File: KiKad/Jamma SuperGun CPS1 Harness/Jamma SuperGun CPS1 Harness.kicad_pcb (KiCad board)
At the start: 2 copper layers, 110.4 x 36 mm, 2 parts

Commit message: updates
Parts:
- renumbered J_FEMALE to J_FEMALE1, J_MALE to J_MALE1
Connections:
- J_FEMALE1 pad 1: (no net) -> /GND
- J_FEMALE1 pad 2: (no net) -> /GND
- J_FEMALE1 pad 3: (no net) -> /+5V
- J_FEMALE1 pad 4: (no net) -> /+5V
- J_FEMALE1 pad 5: (no net) -> /-5V
- J_FEMALE1 pad 6: (no net) -> /+12V
- J_FEMALE1 pad 8: (no net) -> /Coin Counter 1
- J_FEMALE1 pad 9: (no net) -> /Lockout 1
- J_MALE1 pad 1: (no net) -> /GND
- J_MALE1 pad 2: (no net) -> /GND
- J_MALE1 pad 3: (no net) -> /+5V
- J_MALE1 pad 4: (no net) -> /+5V
- J_MALE1 pad 5: (no net) -> /-5V
- J_MALE1 pad 6: (no net) -> /+12V
- J_MALE1 pad 8: (no net) -> /Coin Counter 1
- J_MALE1 pad 9: (no net) -> /Lockout 1
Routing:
- net /GND: track 0.00 -> 162.0 mm
- net /+5V: track 0.00 -> 102.5 mm
- net /-5V: track 0.00 -> 51.3 mm
- net /+12V: track 0.00 -> 51.2 mm
- net /Coin Counter 1: track 0.00 -> 27.0 mm
- net /2P Button 1: track 0.00 -> 26.9 mm
- net /Video Sync: track 0.00 -> 26.9 mm
- net /Video Red: track 0.00 -> 26.9 mm
- net /Video Green: track 0.00 -> 26.9 mm
- net /Video GND: track 0.00 -> 26.9 mm
- net /Video Blue: track 0.00 -> 26.9 mm
- net /Tilt Switch: track 0.00 -> 26.9 mm
- net /Test Switch: track 0.00 -> 26.9 mm
- net /Speaker-: track 0.00 -> 26.9 mm
- net /Speaker+: track 0.00 -> 26.9 mm
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
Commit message: updates
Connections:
- net /1P Button 1 renamed /1P_LP
- net /1P Button 2 renamed /1P_MP
- net /2P Button 1 renamed /2P_LP
- net /2P Button 2 renamed /2P_MP
- J_FEMALE1 pad 24: /1P Button 3 -> /1P_HP
- J_FEMALE1 pad b: /2P Button 3 -> /2P_HP
- J_MALE1 pad 24: /1P Button 3 -> /1P_LK
- J_MALE1 pad 25: /N/C -> /1P_MK
- J_MALE1 pad 26: /N/C -> /1P_HP
- J_MALE1 pad 27: /GND -> /1P_HK
- J_MALE1 pad b: /2P Button 3 -> /2P_LK
- J_MALE1 pad c: /N/C -> /2P_MK
- J_MALE1 pad d: /N/C -> /2P_HP
- J_MALE1 pad e: /GND -> /2P_HK
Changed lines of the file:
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@@
 			(size 2.35 8)
 			(layers "F.Cu" "F.Mask" "F.Paste")
-			(net "/1P Button 1")
+			(net "/1P_LP")
 			(pinfunction "22_22")
 			(pintype "input")
@@
 			(size 2.35 8)
 			(layers "F.Cu" "F.Mask" "F.Paste")
-			(net "/1P Button 2")
+			(net "/1P_MP")
 			(pinfunction "23_23")
 			(pintype "input")
@@
 			(size 2.35 8)
 			(layers "F.Cu" "F.Mask" "F.Paste")
-			(net "/1P Button 3")
+			(net "/1P_HP")
 			(pinfunction "24_24")
 			(pintype "input")
@@
 			(size 2.35 8)
 			(layers "F.Mask" "B.Cu" "F.Paste")
-			(net "/2P Button 1")
+			(net "/2P_LP")
 			(pinfunction "Z_Z")
 			(pintype "input")
@@
 			(size 2.35 8)
 			(layers "F.Mask" "B.Cu" "F.Paste")
-			(net "/2P Button 2")
+			(net "/2P_MP")
 			(pinfunction "a_a")
 			(pintype "input")
@@
 			(size 2.35 8)
 			(layers "F.Mask" "B.Cu" "F.Paste")
-			(net "/2P Button 3")
+			(net "/2P_HP")
 			(pinfunction "b_b")
 			(pintype "input")
@@
 			(size 2.35 8)
 			(layers "F.Cu" "F.Mask" "F.Paste")
-			(net "/1P Button 1")
+			(net "/1P_LP")
 			(pinfunction "22_22")
 			(pintype "input")
@@
 			(size 2.35 8)
 			(layers "F.Cu" "F.Mask" "F.Paste")
-			(net "/1P Button 2")
+			(net "/1P_MP")
 			(pinfunction "23_23")
 			(pintype "input")
@@
 			(size 2.35 8)
 			(layers "F.Cu" "F.Mask" "F.Paste")
-			(net "/1P Button 3")
+			(net "/1P_LK")
 			(pinfunction "24_24")
 			(pintype "input")
@@
 			(size 2.35 8)
 			(layers "F.Cu" "F.Mask" "F.Paste")
-			(net "/N{slash}C")
+			(net "/1P_MK")
 			(pinfunction "25_25")
 			(pintype "input")
@@
 			(size 2.35 8)
 			(layers "F.Cu" "F.Mask" "F.Paste")
-			(net "/N{slash}C")
+			(net "/1P_HP")
 			(pinfunction "26_26")
 			(pintype "input")
@@
 			(size 2.35 8)
 			(layers "F.Cu" "F.Mask" "F.Paste")
-			(net "/GND")
+			(net "/1P_HK")
 			(pinfunction "27_27")
 			(pintype "input")
@@
 			(size 2.35 8)
 			(layers "F.Mask" "B.Cu" "F.Paste")
-			(net "/2P Button 1")
+			(net "/2P_LP")
 			(pinfunction "Z_Z")
 			(pintype "input")
@@
 			(size 2.35 8)
 			(layers "F.Mask" "B.Cu" "F.Paste")
-			(net "/2P Button 2")
+			(net "/2P_MP")
 			(pinfunction "a_a")
 			(pintype "input")
@@
 			(size 2.35 8)
 			(layers "F.Mask" "B.Cu" "F.Paste")
-			(net "/2P Button 3")
+			(net "/2P_LK")
 			(pinfunction "b_b")
 			(pintype "input")
@@
 			(size 2.35 8)
 			(layers "F.Mask" "B.Cu" "F.Paste")
-			(net "/N{slash}C")
+			(net "/2P_MK")
 			(pinfunction "c_c")
 			(pintype "input")
@@
 			(size 2.35 8)
 			(layers "F.Mask" "B.Cu" "F.Paste")
-			(net "/N{slash}C")
+			(net "/2P_HP")
 			(pinfunction "d_d")
 			(pintype "input")
@@
 			(size 2.35 8)
 			(layers "F.Mask" "B.Cu" "F.Paste")
-			(net "/GND")
+			(net "/2P_HK")
 			(pinfunction "e_e")
 			(pintype "input")
@@
 	)
 	(segment
-		(start 179.39 46)
-		(end 179.39 72.9)
-		(width 0.4)
-		(layer "F.Cu")
-		(net "/Speaker+")
-	)
-	(segment
-		(start 183.35 46)
-		(end 183.35 72.9)
-		(width 0.4)
-		(layer "F.Cu")
-		(net "/Audio+")
-	)
-	(segment
-		(start 187.31 46)
-		(end 187.31 72.9)
-		(width 0.4)
-		(layer "F.Cu")
-		(net "/Video Red")
-	)
-	(segment
-		(start 191.27 46)
-		(end 191.27 72.9)
-		(width 0.4)
-		(layer "F.Cu")
-		(net "/Video Blue")
-	)
-	(segment
-		(start 195.23 46)
-		(end 195.23 72.9)
-		(width 0.4)
-		(layer "F.Cu")
-		(net "/Video GND")
-	)
-	(segment
-		(start 199.19 46)
-		(end 199.19 72.9)
-		(width 0.4)
-		(layer "F.Cu")
-		(net "/Test Switch")
-	)
-	(segment
-		(start 203.15 46)
-		(end 203.15 72.9)
-		(width 0.4)
-		(layer "F.Cu")
-		(net "/1P Coin")
-	)
-	(segment
-		(start 207.11 46)
-		(end 207.11 72.9)
-		(width 0.4)
-		(layer "F.Cu")
-		(net "/1P Start")
-	)
-	(segment
-		(start 211.07 46)
-		(end 211.07 72.9)
-		(width 0.4)
-		(layer "F.Cu")
-		(net "/1P Up")
-	)
-	(segment
-		(start 215.03 46)
-		(end 215.03 72.9)
-		(width 0.4)
-		(layer "F.Cu")
-		(net "/1P Down")
-	)
-	(segment
-		(start 218.99 46)
-		(end 218.99 72.9)
-		(width 0.4)
-		(layer "F.Cu")
-		(net "/1P Left")
-	)
-	(segment
-		(start 222.95 46)
-		(end 222.95 72.9)
-		(width 0.4)
-		(layer "F.Cu")
-		(net "/1P Right")
-	)
-	(segment
-		(start 226.91 46)
-		(end 226.91 72.9)
-		(width 0.4)
-		(layer "F.Cu")
-		(net "/1P Button 1")
-	)
-	(segment
-		(start 230.87 46)
-		(end 230.87 72.9)
-		(width 0.4)
-		(layer "F.Cu")
-		(net "/1P Button 2")
-	)
-	(segment
 		(start 147.6 48.525)
 		(end 147.6 72.875)
@@
 	)
 	(segment
+		(start 171.47 46.03)
+		(end 171.4 46.1)
+		(width 0.2)
+		(layer "F.Cu")
+		(net "/Coin Counter 1")
+	)
+	(segment
+		(start 171.4 46.1)
+		(end 171.47 46.17)
+		(width 0.2)
+		(layer "F.Cu")
+		(net "/Coin Counter 1")
+	)
+	(segment
+		(start 171.47 46)
+		(end 171.47 46.03)
+		(width 0.2)
+		(layer "F.Cu")
+		(net "/Coin Counter 1")
+	)
+	(segment
+		(start 171.47 46.17)
+		(end 171.47 72.9)
+		(width 0.4)
+		(layer "F.Cu")
+		(net "/Coin Counter 1")
+	)
+	(segment
+		(start 175.43 46)
+		(end 175.43 72.9)
+		(width 0.4)
+		(layer "F.Cu")
+		(net "/Lockout 1")
+	)
+	(segment
+		(start 179.39 46)
+		(end 179.39 72.9)
+		(width 0.4)
+		(layer "F.Cu")
+		(net "/Speaker+")
+	)
+	(segment
+		(start 183.35 46)
+		(end 183.35 72.9)
+		(width 0.4)
+		(layer "F.Cu")
+		(net "/Audio+")
+	)
+	(segment
+		(start 187.31 46)
+		(end 187.31 72.9)
+		(width 0.4)
+		(layer "F.Cu")
+		(net "/Video Red")
+	)
+	(segment
+		(start 191.27 46)
+		(end 191.27 72.9)
+		(width 0.4)
+		(layer "F.Cu")
+		(net "/Video Blue")
+	)
+	(segment
+		(start 195.23 46)
+		(end 195.23 72.9)
+		(width 0.4)
+		(layer "F.Cu")
+		(net "/Video GND")
+	)
+	(segment
+		(start 199.19 46)
+		(end 199.19 72.9)
+		(width 0.4)
+		(layer "F.Cu")
+		(net "/Test Switch")
+	)
+	(segment
+		(start 203.15 46)
+		(end 203.15 72.9)
+		(width 0.4)
+		(layer "F.Cu")
+		(net "/1P Coin")
+	)
+	(segment
+		(start 207.11 46)
+		(end 207.11 72.9)
+		(width 0.4)
+		(layer "F.Cu")
+		(net "/1P Start")
+	)
+	(segment
+		(start 211.07 46)
+		(end 211.07 72.9)
+		(width 0.4)
+		(layer "F.Cu")
+		(net "/1P Up")
+	)
+	(segment
+		(start 215.03 46)
+		(end 215.03 72.9)
+		(width 0.4)
+		(layer "F.Cu")
+		(net "/1P Down")
+	)
+	(segment
+		(start 218.99 46)
+		(end 218.99 72.9)
+		(width 0.4)
+		(layer "F.Cu")
+		(net "/1P Left")
+	)
+	(segment
+		(start 222.95 46)
+		(end 222.95 72.9)
+		(width 0.4)
+		(layer "F.Cu")
+		(net "/1P Right")
+	)
+	(segment
 		(start 171.47 46)
 		(end 171.47 72.9)
@@
 		(width 0.4)
 		(layer "B.Cu")
-		(net "/2P Button 1")
+		(net "/2P_LP")
 	)
 	(segment
@@
 		(width 0.2)
 		(layer "B.Cu")
-		(net "/2P Button 1")
+		(net "/2P_LP")
 	)
 	(segment
@@
 		(width 0.2)
 		(layer "B.Cu")
-		(net "/2P Button 1")
+		(net "/2P_LP")
 	)
 	(segment
@@
 		(width 0.2)
 		(layer "B.Cu")
-		(net "/2P Button 1")
+		(net "/2P_LP")
+	)
+	(segment
+		(start 226.91 46)
+		(end 226.91 72.9)
+		(width 0.4)
+		(layer "F.Cu")
+		(net "/1P_LP")
 	)
 	(segment
@@
 		(width 0.4)
 		(layer "B.Cu")
-		(net "/2P Button 2")
-	)
-	(segment
-		(start 175.43 46)
-		(end 175.43 72.9)
-		(width 0.4)
-		(layer "F.Cu")
-		(net "/Lockout 1")
-	)
-	(segment
-		(start 171.47 46.03)
-		(end 171.4 46.1)
-		(width 0.2)
-		(layer "F.Cu")
-		(net "/Coin Counter 1")
-	)
-	(segment
-		(start 171.4 46.1)
-		(end 171.47 46.17)
-		(width 0.2)
-		(layer "F.Cu")
-		(net "/Coin Counter 1")
-	)
-	(segment
-		(start 171.47 46)
-		(end 171.47 46.03)
-		(width 0.2)
-		(layer "F.Cu")
-		(net "/Coin Counter 1")
-	)
-	(segment
-		(start 171.47 46.17)
-		(end 171.47 72.9)
-		(width 0.4)
-		(layer "F.Cu")
-		(net "/Coin Counter 1")
+		(net "/2P_MP")
+	)
+	(segment
+		(start 230.87 46)
+		(end 230.87 72.9)
+		(width 0.4)
+		(layer "F.Cu")
+		(net "/1P_MP")
 	)
 	(embedded_fonts no)

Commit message: updates
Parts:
- added CPS1_KH1: ~, Connector_JST:JST_EH_B10B-EH-A_1x10_P2.50mm_Vertical, F.Cu at (249.1, 58.8)
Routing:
- net /2P_HP: track 0.00 -> 61.5 mm
- net /1P_HP: track 0.00 -> 60.4 mm, vias 0 -> 2
- net /2P_HK: track 0.00 -> 28.0 mm
- net /1P_MP: track 26.9 -> 48.9 mm
- net /2P_MP: track 26.9 -> 48.3 mm
- net /1P_HK: track 0.00 -> 19.8 mm, vias 0 -> 2
- net /2P_MK: track 0.00 -> 19.7 mm, vias 0 -> 2
- net /1P_LK: track 0.00 -> 18.1 mm
- net /1P_MK: track 0.00 -> 17.2 mm, vias 0 -> 2
- net /1P_LP: track 26.9 -> 44.0 mm
- net /2P_LP: track 26.9 -> 44.0 mm
- net /1P Right: track 26.9 -> 41.1 mm
- net /2P Right: track 26.9 -> 41.1 mm
- net /2P_LK: track 0.00 -> 13.1 mm, vias 0 -> 2
- net /GND: track 162.0 -> 170.1 mm
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
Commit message: updates
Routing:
- net /1P_MP: track 48.9 -> 48.3 mm
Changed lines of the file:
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@@
+	)
+	(segment
+		(start 222.43 66.43)
+		(end 222.95 66.95)
+		(width 0.4)
+		(layer "F.Cu")
+		(net "/1P Right")
+	)
+	(segment
+		(start 216.48 66.43)
+		(end 222.43 66.43)
+		(width 0.4)
+		(layer "F.Cu")
+		(net "/1P Right")
+	)
+	(segment
+		(start 222.95 66.95)
+		(end 222.95 72.9)
+		(width 0.4)
+		(layer "F.Cu")
+		(net "/1P Right")
+	)
+	(segment
+		(start 213.57 55.38)
+		(end 213.57 63.52)
+		(width 0.4)
+		(layer "F.Cu")
+		(net "/1P Right")
 	)
 	(segment
@@
 	)
 	(segment
-		(start 216.05 66)
-		(end 222 66)
+		(start 213.57 63.52)
+		(end 216.48 66.43)
+		(width 0.4)
+		(layer "F.Cu")
+		(net "/1P Right")
+	)
+	(segment
+		(start 217.95 51)
+		(end 213.57 55.38)
 		(width 0.4)
 		(layer "F.Cu")
@@
 	)
 	(segment
-		(start 213.57 63.52)
-		(end 216.05 66)
-		(width 0.4)
-		(layer "F.Cu")
-		(net "/1P Right")
-	)
-	(segment
-		(start 213.57 55.38)
-		(end 213.57 63.52)
-		(width 0.4)
-		(layer "F.Cu")
-		(net "/1P Right")
-	)
-	(segment
-		(start 222.95 66.95)
-		(end 222.95 72.9)
-		(width 0.4)
-		(layer "F.Cu")
-		(net "/1P Right")
-	)
-	(segment
-		(start 217.95 51)
-		(end 213.57 55.38)
-		(width 0.4)
-		(layer "F.Cu")
-		(net "/1P Right")
-	)
-	(segment
-		(start 222 66)
-		(end 222.95 66.95)
-		(width 0.4)
-		(layer "F.Cu")
-		(net "/1P Right")
+		(start 226.91 46)
+		(end 226.91 50.296)
+		(width 0.4)
+		(layer "F.Cu")
+		(net "/1P_LP")
+	)
+	(segment
+		(start 214.84 62.84)
+		(end 217 65)
+		(width 0.4)
+		(layer "F.Cu")
+		(net "/1P_LP")
+	)
+	(segment
+		(start 225.206 52)
+		(end 219.182 52)
+		(width 0.4)
+		(layer "F.Cu")
+		(net "/1P_LP")
 	)
 	(segment
@@
 	)
 	(segment
+		(start 226.91 68.91)
+		(end 226.91 72.9)
+		(width 0.4)
+		(layer "F.Cu")
+		(net "/1P_LP")
+	)
+	(segment
 		(start 217 65)
 		(end 223 65)
@@
 	)
 	(segment
-		(start 214.84 62.84)
-		(end 217 65)
-		(width 0.4)
-		(layer "F.Cu")
-		(net "/1P_LP")
-	)
-	(segment
-		(start 214.84 56.16)
-		(end 214.84 62.84)
-		(width 0.4)
-		(layer "F.Cu")
-		(net "/1P_LP")
-	)
-	(segment
-		(start 225.206 52)
-		(end 219 52)
-		(width 0.4)
-		(layer "F.Cu")
-		(net "/1P_LP")
-	)
-	(segment
-		(start 226.91 46)
-		(end 226.91 50.296)
-		(width 0.4)
-		(layer "F.Cu")
-		(net "/1P_LP")
-	)
-	(segment
-		(start 226.91 68.91)
-		(end 226.91 72.9)
-		(width 0.4)
-		(layer "F.Cu")
-		(net "/1P_LP")
-	)
-	(segment
-		(start 219 52)
-		(end 214.84 56.16)
+		(start 219.182 52)
+		(end 214.84 56.342)
 		(width 0.4)
 		(layer "F.Cu")
@@
 	)
 	(segment
+		(start 214.84 56.342)
+		(end 214.84 62.84)
+		(width 0.4)
+		(layer "F.Cu")
+		(net "/1P_LP")
+	)
+	(segment
+		(start 218.638528 63.89)
+		(end 226.016 63.89)
+		(width 0.4)
+		(layer "F.Cu")
+		(net "/1P_MP")
+	)
+	(segment
 		(start 219.4812 53.0188)
 		(end 216.11 56.39)
@@
 	)
 	(segment
-		(start 218.536928 63.7884)
-		(end 225.9144 63.7884)
-		(width 0.4)
-		(layer "F.Cu")
-		(net "/1P_MP")
-	)
-	(segment
-		(start 230.87 50.908)
-		(end 228.7592 53.0188)
+		(start 226.016 63.89)
+		(end 230.87 68.744)
+		(width 0.4)
+		(layer "F.Cu")
+		(net "/1P_MP")
+	)
+	(segment
+		(start 230.87 49.892)
+		(end 227.7432 53.0188)
+		(width 0.4)
+		(layer "F.Cu")
+		(net "/1P_MP")
+	)
+	(segment
+		(start 227.7432 53.0188)
+		(end 219.4812 53.0188)
+		(width 0.4)
+		(layer "F.Cu")
+		(net "/1P_MP")
+	)
+	(segment
+		(start 216.11 61.361472)
+		(end 218.638528 63.89)
 		(width 0.4)
 		(layer "F.Cu")
@@
 	(segment
 		(start 230.87 46)
-		(end 230.87 50.908)
-		(width 0.4)
-		(layer "F.Cu")
-		(net "/1P_MP")
-	)
-	(segment
-		(start 228.7592 53.0188)
-		(end 219.4812 53.0188)
-		(width 0.4)
-		(layer "F.Cu")
-		(net "/1P_MP")
-	)
-	(segment
-		(start 216.11 61.361472)
-		(end 218.536928 63.7884)
-		(width 0.4)
-		(layer "F.Cu")
-		(net "/1P_MP")
-	)
-	(segment
-		(start 225.9144 63.7884)
-		(end 230.87 68.744)
+		(end 230.87 49.892)
 		(width 0.4)
 		(layer "F.Cu")
@@
 	)
 	(segment
-		(start 216.05 66)
-		(end 222.03 66)
+		(start 213.57 63.52)
+		(end 216.48 66.43)
+		(width 0.4)
+		(layer "B.Cu")
+		(net "/2P Right")
+	)
+	(segment
+		(start 222.95 66.92)
+		(end 222.95 72.9)
+		(width 0.4)
+		(layer "B.Cu")
+		(net "/2P Right")
+	)
+	(segment
+		(start 216.48 66.43)
+		(end 222.46 66.43)
+		(width 0.4)
+		(layer "B.Cu")
+		(net "/2P Right")
+	)
+	(segment
+		(start 222.95 46)
+		(end 222.95 51)
+		(width 0.4)
+		(layer "B.Cu")
+		(net "/2P Right")
+	)
+	(segment
+		(start 222.46 66.43)
+		(end 222.95 66.92)
+		(width 0.4)
+		(layer "B.Cu")
+		(net "/2P Right")
+	)
+	(segment
+		(start 218 51)
+		(end 213.57 55.43)
+		(width 0.4)
+		(layer "B.Cu")
+		(net "/2P Right")
+	)
+	(segment
+		(start 222.95 51)
+		(end 218 51)
 		(width 0.4)
 		(layer "B.Cu")
@@
 		(width 0.4)
 		(layer "B.Cu")
-		(net "/2P Right")
-	)
-	(segment
-		(start 222.03 66)
-		(end 222.95 66.92)
-		(width 0.4)
-		(layer "B.Cu")
-		(net "/2P Right")
-	)
-	(segment
-		(start 213.57 63.52)
-		(end 216.05 66)
-		(width 0.4)
-		(layer "B.Cu")
-		(net "/2P Right")
-	)
-	(segment
-		(start 222.95 51)
-		(end 218 51)
-		(width 0.4)
-		(layer "B.Cu")
-		(net "/2P Right")
-	)
-	(segment
-		(start 218 51)
-		(end 213.57 55.43)
-		(width 0.4)
-		(layer "B.Cu")
-		(net "/2P Right")
-	)
-	(segment
-		(start 222.95 66.92)
-		(end 222.95 72.9)
-		(width 0.4)
-		(layer "B.Cu")
-		(net "/2P Right")
-	)
-	(segment
-		(start 222.95 46)
-		(end 222.95 51)
-		(width 0.4)
-		(layer "B.Cu")

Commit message: updates
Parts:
- moved CPS1_KH1 3.45 mm to (245.9, 60.1)
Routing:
- net /GND: track 170.1 -> 202.2 mm
- net /2P_LK: track 13.1 -> 19.2 mm
- net /1P_MK: track 17.2 -> 22.2 mm
- net /1P_HK: track 19.8 -> 22.3 mm
- net /2P_HK: track 28.0 -> 30.3 mm

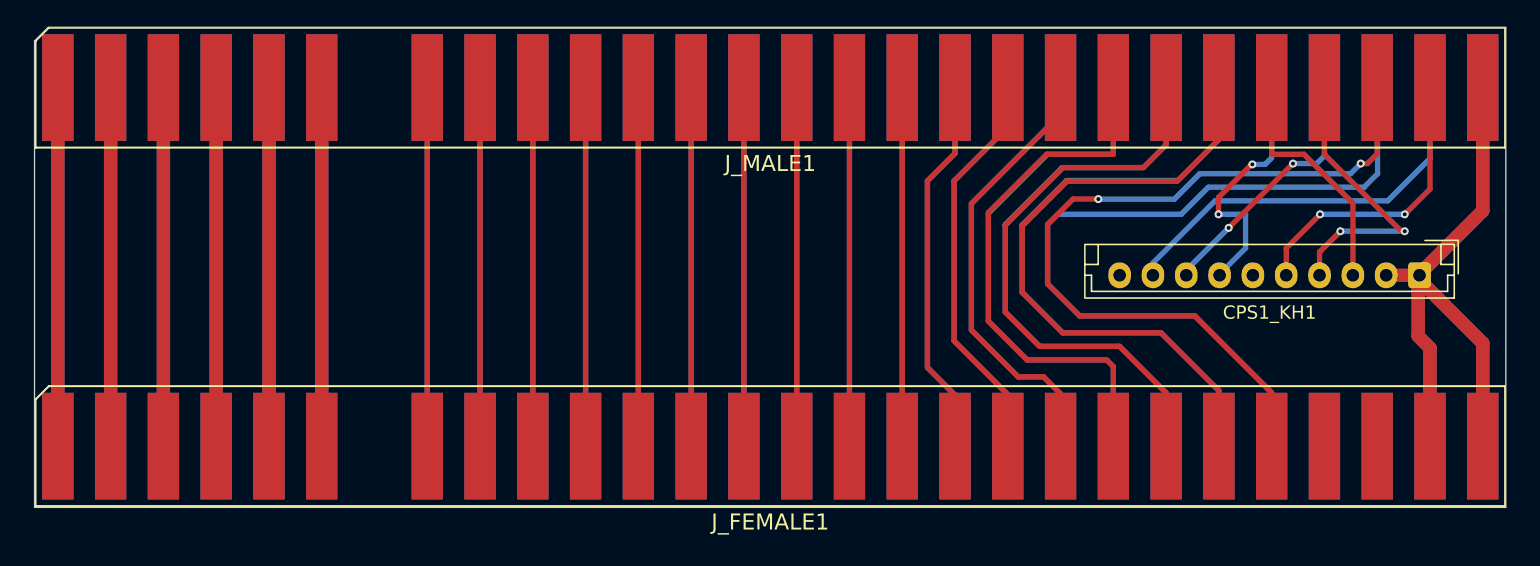
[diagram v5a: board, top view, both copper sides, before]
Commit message: update size
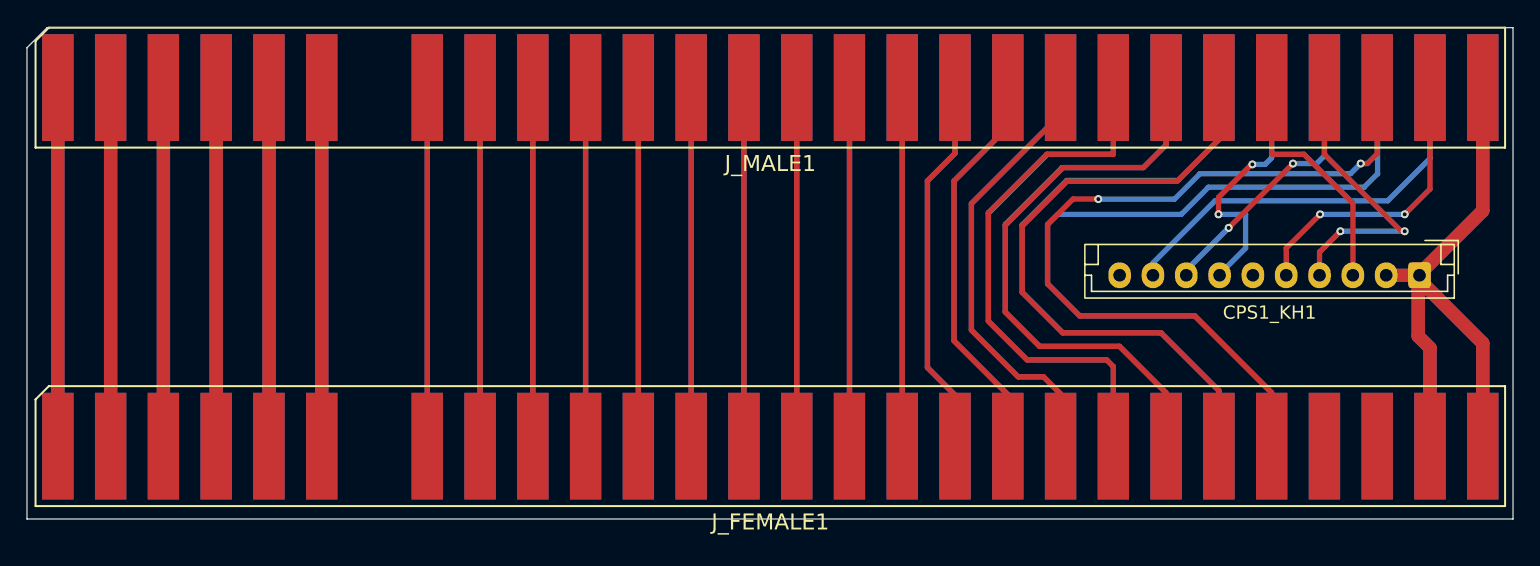
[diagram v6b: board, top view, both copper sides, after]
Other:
- board size 110.4 x 36 mm -> 111.5 x 36.9 mm
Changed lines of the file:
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@@
 	(gr_poly
 		(pts
-			(xy 142 77.5) (xy 252.4 77.5) (xy 252.4 41.5) (xy 143 41.5) (xy 142 42.5)
+			(xy 141.434 78.368) (xy 252.94 78.368) (xy 252.94 41.5) (xy 142.942 41.5) (xy 141.434 43.008)
 		)
 		(stroke
